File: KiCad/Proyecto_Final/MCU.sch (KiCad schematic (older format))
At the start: 5 parts

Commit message: Definido MCU, agregado datasheet y librerias.
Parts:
- removed U?: STM32F723VCTx, Package_QFP:LQFP-100_14x14mm_P0.5mm, symbol Tesis2020-21:STM32F723VCTx
- added C?: 2.2uF, symbol Device:C
- added C? (x10): 100nF, symbol Device:C
- added C?: 4.7uF, symbol Device:C
- added R?: 3k 1%, symbol Device:R
- added U?: STM32F723ZCTx, Package_QFP:LQFP-144_20x20mm_P0.5mm, symbol MCU_ST_STM32F7:STM32F723ZCTx
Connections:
- net labels added: RCC_OSC_IN, RCC_OSC_OUT, USB_OTG_HS_DM, USB_OTG_HS_DP, VDD, VSS
- wire segments 29 -> 85

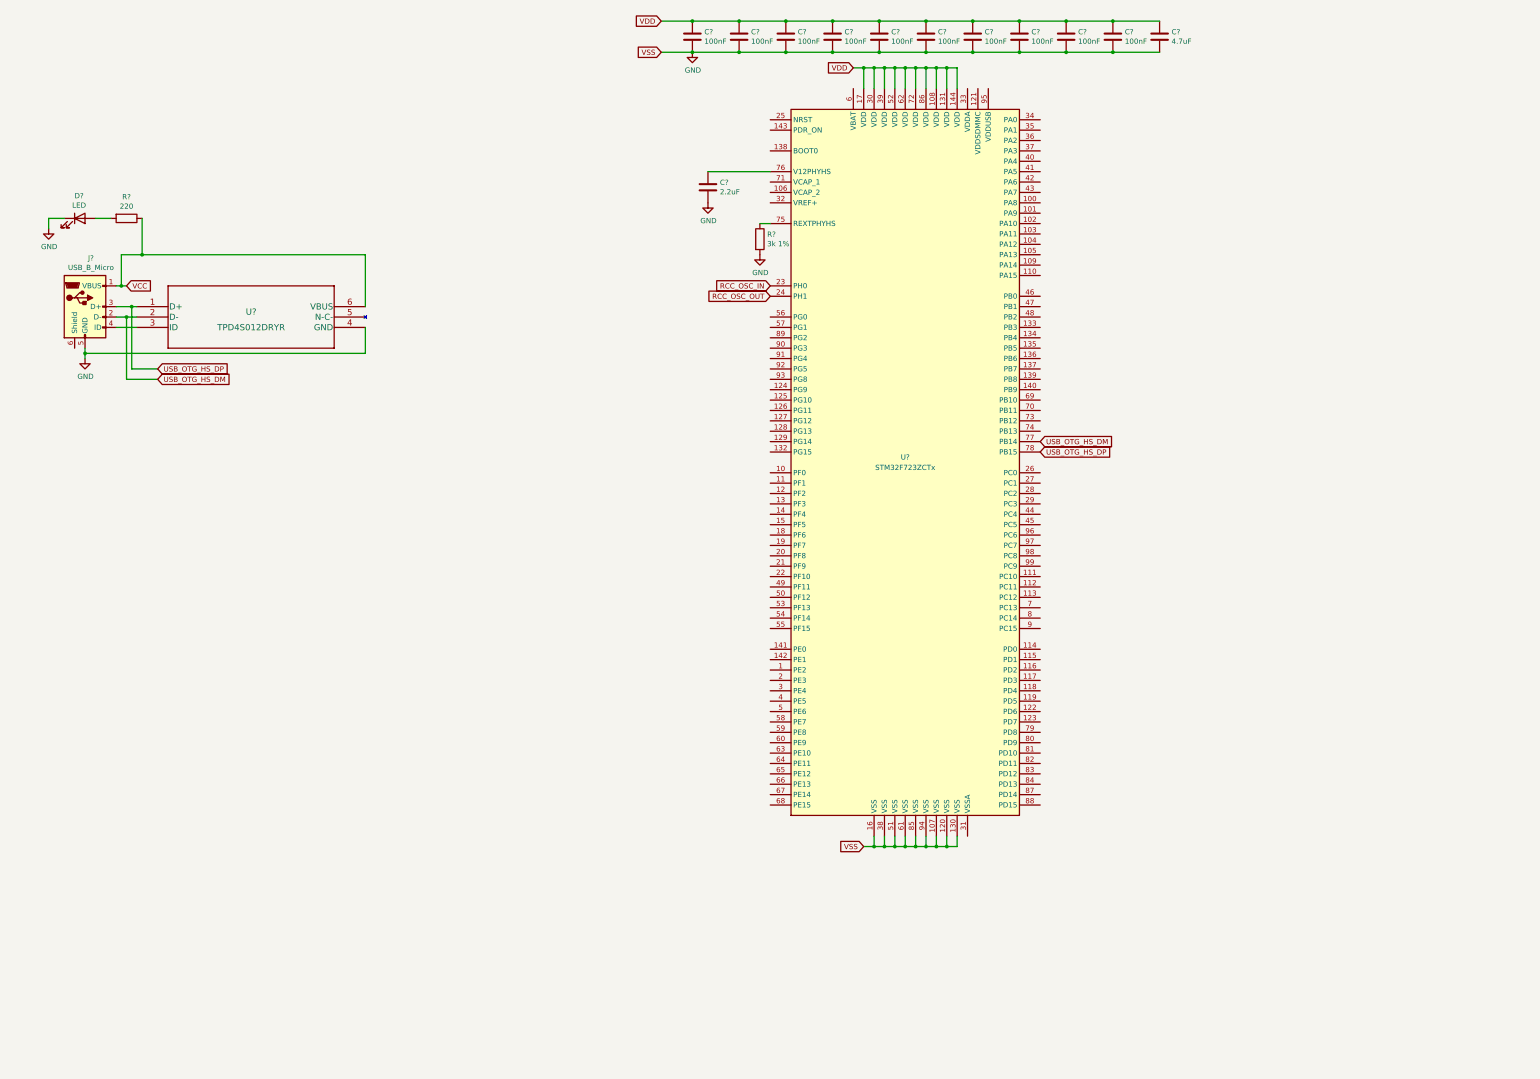
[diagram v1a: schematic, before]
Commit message: Actualización hoja MCU y latex.
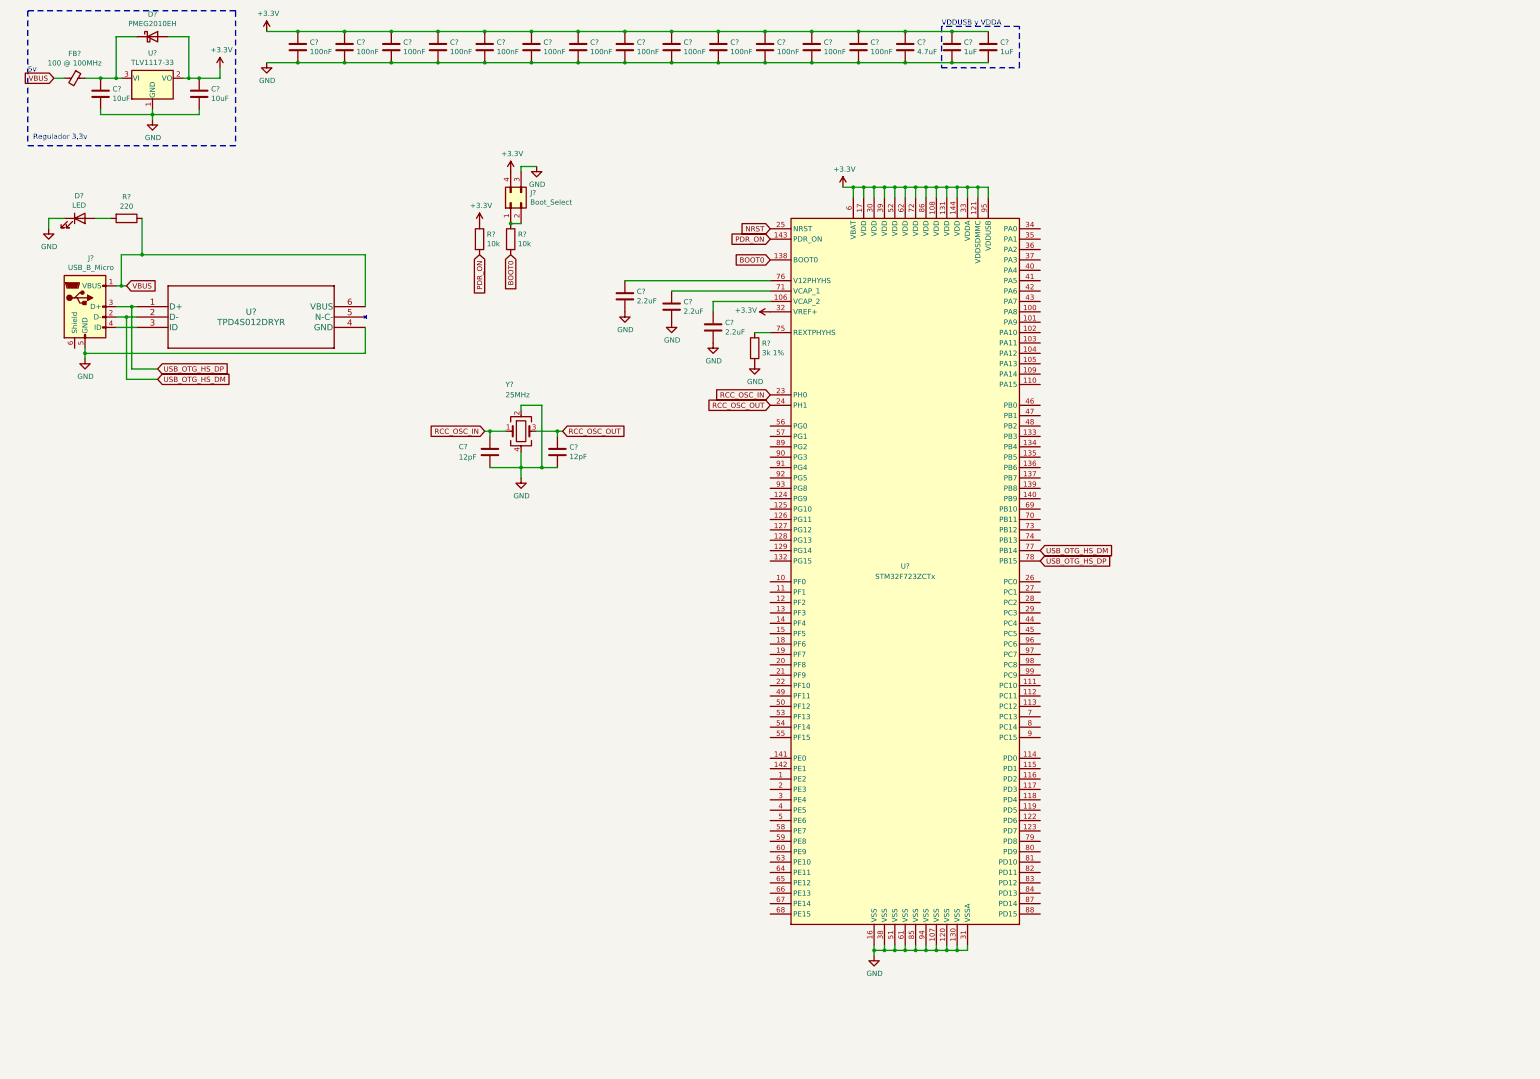
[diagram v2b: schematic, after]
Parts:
- added C? (x2): 10uF, symbol Device:C
- added C? (x3): 100nF, symbol Device:C
- added C? (x2): 2.2uF, symbol Device:C
- added C? (x2): 1uF, symbol Device:C
- added C? (x2): 12pF, symbol Device:C
- added D?: PMEG2010EH, Diode_SMD:D_SOD-123F, symbol Diode:PMEG2010EH
- added FB?: 100 @ 100MHz, symbol Device:Ferrite_Bead_Small
- added J?: Boot_Select, symbol Connector_Generic:Conn_02x02_Counter_Clockwise
- added R? (x2): 10k, symbol Device:R
- added U?: TLV1117-33, symbol Regulator_Linear:TLV1117-33
- added Y?: 25MHz, symbol Device:Crystal_GND24
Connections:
- net VDD is gone; now on net +3V3: C?.1, C?.1, C?.1, C?.1, C?.1, C?.1, C?.1, C?.1, C?.1, C?.1, C?.1, U?.108 (VDD), U?.131 (VDD), U?.144 (VDD), U?.17 (VDD), U?.30 (VDD), U?.39 (VDD), U?.52 (VDD), U?.62 (VDD), U?.72 (VDD), U?.86 (VDD)
- net GND: now also U?.31 (VSSA), C?.2, C?.2, C?.2, C?.2, C?.2, C?.2, C?.2, C?.2, C?.2, C?.2, C?.2, J?.3 (Pin_3), U?.1 (GND), Y?.2, Y?.4
- net RCC_OSC_IN: now also C?.1, Y?.1
- net RCC_OSC_OUT: now also C?.1, Y?.3
- net at U?.106 (VCAP_2): now also C?.1
- net +3V3: now reaches U?.121 (VDDSDMMC)
- net +3V3: now also U?.32 (VREF+), U?.33 (VDDA), U?.6 (VBAT), U?.95 (VDDUSB), C?.1, C?.1, C?.1, C?.1, C?.1, C?.1, D?.2 (A), J?.4 (Pin_4), R?.1, U?.2 (VO)
- net BOOT0: now reaches U?.138 (BOOT0)
- net BOOT0: now also R?.2
- net PDR_ON: now reaches U?.143 (PDR_ON)
- net PDR_ON: now also R?.2
- net NRST: now reaches U?.25 (NRST)
- net at U?.71 (VCAP_1): now also C?.1
- net VCC renamed VBUS
- net VBUS: now also FB?.2
- new net: C?.1, D?.1 (K), FB?.1, U?.3 (VI)
- new net: J?.1 (Pin_1), J?.2 (Pin_2), R?.1
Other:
- note added: "5v"
- note added: "Regulador 3,3v"
- note added: "VDDUSB y VDDA"
- moved on the sheet: C?, R?, U?

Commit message: backup/update
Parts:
- removed R?: 220, symbol Device:R
- added J?: ARM SWD, symbol Connector_Generic:Conn_02x05_Odd_Even
- added R?: 2.2k, symbol Device:R
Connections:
- net +3V3: now also D?.2 (A), J?.1 (Pin_1)
- net GND: now also J?.3 (Pin_3), J?.5 (Pin_5), J?.9 (Pin_9), R?.2; no longer D?.1 (K)
- net NRST: now also J?.10 (Pin_10)
- net SWDIO: now reaches U?.105 (PA13)
- net SWDIO: now also J?.2 (Pin_2)
- net SWCLK: now reaches U?.109 (PA14)
- net SWCLK: now also J?.4 (Pin_4)
- net SWO: now reaches U?.133 (PB3)
- net SWO: now also J?.6 (Pin_6)
- new net: D?.1 (K), R?.1
- no-connect marks 0 -> 2
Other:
- note added: "Falta:\n- SPI\n- I2C\n- GPIO"
- moved on the sheet: C?, D?

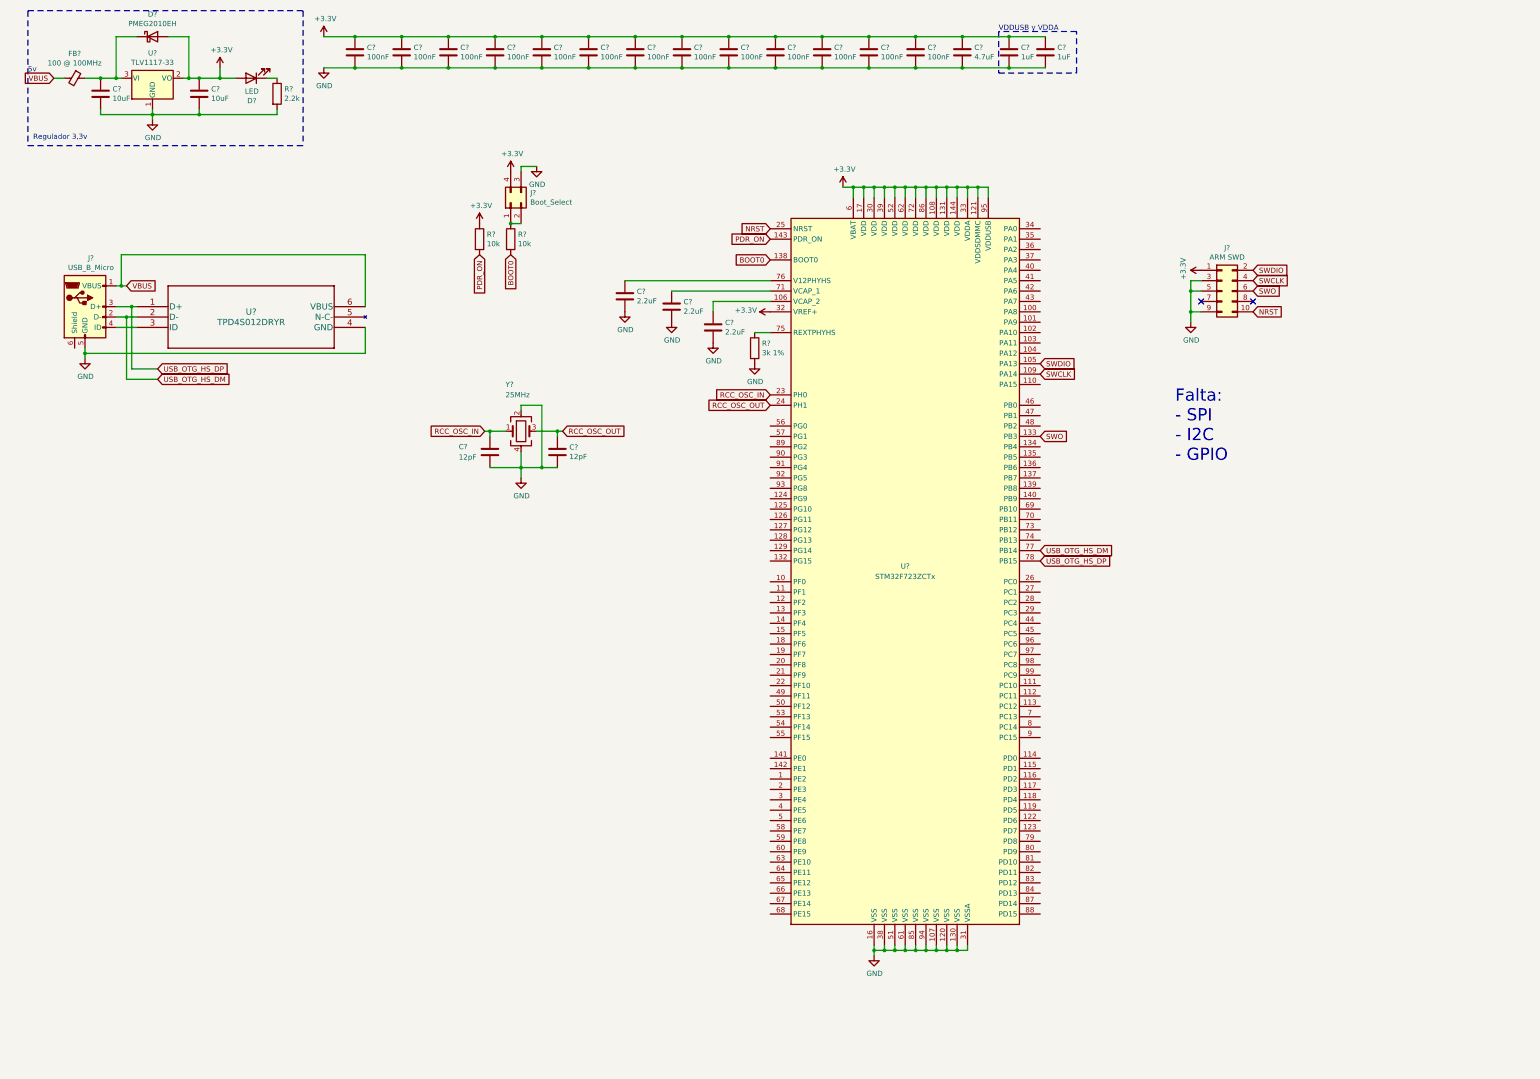
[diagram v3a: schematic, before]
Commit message: Cambio nombre de datasheets para búsqueda rápida, actualizada hoja MCU, modificadas hojas de frontend y transceptor.
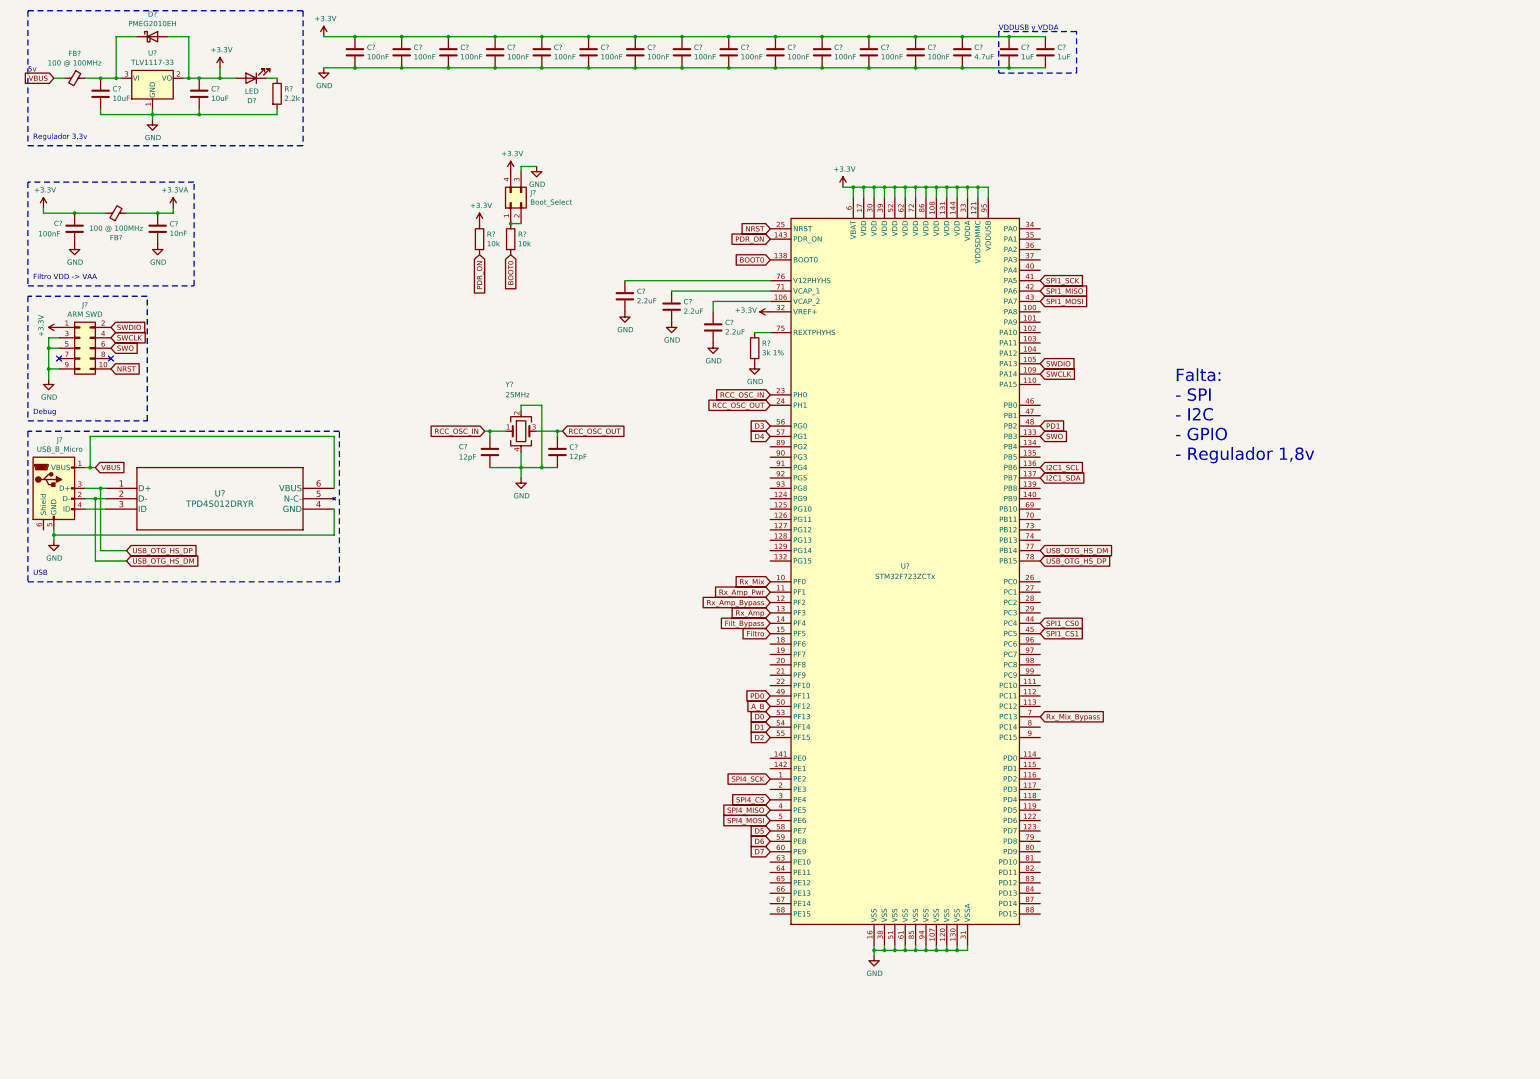
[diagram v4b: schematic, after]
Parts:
- added C?: 100nF, symbol Device:C
- added C?: 10nF, symbol Device:C
- added FB?: 100 @ 100MHz, symbol Device:Ferrite_Bead_Small
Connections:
- net +3V3: now also C?.1, FB?.1
- net GND: now also C?.2, C?.2
- net SPI4_SCK: now reaches U?.1 (PE2)
- net Rx_Mix: now reaches U?.10 (PF0)
- net Rx_Amp_Pwr: now reaches U?.11 (PF1)
- net Rx_Amp_Bypass: now reaches U?.12 (PF2)
- net Rx_Amp: now reaches U?.13 (PF3)
- net I2C1_SCL: now reaches U?.136 (PB6)
- net I2C1_SDA: now reaches U?.137 (PB7)
- net Filt_Bypass: now reaches U?.14 (PF4)
- net Filtro: now reaches U?.15 (PF5)
- net SPI4_CS: now reaches U?.3 (PE4)
- net SPI4_MISO: now reaches U?.4 (PE5)
- net SPI1_SCK: now reaches U?.41 (PA5)
- net SPI1_MISO: now reaches U?.42 (PA6)
- net SPI1_MOSI: now reaches U?.43 (PA7)
- net SPI1_CS0: now reaches U?.44 (PC4)
- net SPI1_CS1: now reaches U?.45 (PC5)
- net PD1: now reaches U?.48 (PB2)
- net PD0: now reaches U?.49 (PF11)
- net SPI4_MOSI: now reaches U?.5 (PE6)
- net A_B: now reaches U?.50 (PF12)
- net D0: now reaches U?.53 (PF13)
- net D1: now reaches U?.54 (PF14)
- net D2: now reaches U?.55 (PF15)
- net D3: now reaches U?.56 (PG0)
- net D4: now reaches U?.57 (PG1)
- net D5: now reaches U?.58 (PE7)
- net D6: now reaches U?.59 (PE8)
- net D7: now reaches U?.60 (PE9)
- net Rx_Mix_Bypass: now reaches U?.7 (PC13)
- new net +3.3VA: C?.1, FB?.2
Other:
- note added: "Debug"
- note added: "Falta:\n- SPI\n- I2C\n- GPIO\n- Regulador 1,8v"
- note added: "Filtro VDD -> VAA"
- note added: "USB"
- note removed: "Falta:\n- SPI\n- I2C\n- GPIO"
- moved on the sheet: J?, U?

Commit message: Update hoja MCU y transceptor.
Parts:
- added C?: 100nF, symbol Device:C
- added SW?: Reset, symbol Switch:SW_Push_Dual
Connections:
- net GND: now also C?.1, SW?.2, SW?.4
- net NRST: now also C?.2, SW?.1, SW?.3
- net RSSI: now reaches U?.28 (PC2)
- net Trx_Enable: now reaches U?.46 (PB0)
- net Trx_Rx_Enable: now reaches U?.47 (PB1)
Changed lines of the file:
@@
 Text GLabel 10450 7350 2    50   Input ~ 0
 Rx_Mix_Bypass
+$Comp
+L Device:C C?
+U 1 1 6073CF3E
+P 4200 2900
+F 0 "C?" V 4350 2900 50  0000 C CNN
+F 1 "100nF" V 4450 2900 50  0000 C CNN
+F 2 "" H 4238 2750 50  0001 C CNN
+F 3 "~" H 4200 2900 50  0001 C CNN
+	1    4200 2900
+	0    1    1    0
+$EndComp
+Wire Wire Line
+	4350 2900 4500 2900
+Wire Wire Line
+	4050 2900 3900 2900
+Text GLabel 3800 2550 0    50   Input ~ 0
+NRST
+Wire Wire Line
+	3800 2550 3900 2550
+$Comp
+L power:GND #PWR?
+U 1 1 607545DD
+P 4650 2650
+F 0 "#PWR?" H 4650 2400 50  0001 C CNN
+F 1 "GND" H 4655 2477 50  0000 C CNN
+F 2 "" H 4650 2650 50  0001 C CNN
+F 3 "" H 4650 2650 50  0001 C CNN
+	1    4650 2650
+	1    0    0    -1
+$EndComp
+Wire Wire Line
+	4650 2650 4650 2550
+Wire Wire Line
+	4650 2550 4500 2550
+Wire Wire Line
+	3900 2550 3900 2750
+Wire Wire Line
+	4500 2550 4500 2750
+$Comp
+L Switch:SW_Push_Dual SW?
+U 1 1 6076D631
+P 4200 2550
+F 0 "SW?" H 4200 2835 50  0000 C CNN
+F 1 "Reset" H 4200 2744 50  0000 C CNN
+F 2 "" H 4200 2750 50  0001 C CNN
+F 3 "~" H 4200 2750 50  0001 C CNN
+	1    4200 2550
+	1    0    0    -1
+$EndComp
+Wire Wire Line
+	4000 2550 3900 2550
+Connection ~ 3900 2550
+Wire Wire Line
+	4000 2750 3900 2750
+Connection ~ 3900 2750
+Wire Wire Line
+	3900 2750 3900 2900
+Wire Wire Line
+	4400 2750 4500 2750
+Connection ~ 4500 2750
+Wire Wire Line
+	4500 2750 4500 2900
+Wire Wire Line
+	4400 2550 4500 2550
+Connection ~ 4500 2550
+Text GLabel 10450 4350 2    50   Input ~ 0
+Trx_Enable
+Text GLabel 10450 4450 2    50   Input ~ 0
+Trx_Rx_Enable
+Text GLabel 10450 6250 2    50   Input ~ 0
+RSSI
 $EndSCHEMATC
